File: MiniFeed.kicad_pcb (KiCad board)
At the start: 2 copper layers, 100 x 44.4 mm, 91 parts, among them J1 Debug, J2 Connector_1, J3 Uart, J4 Connector_2, M1 Motor_DC, SW1 SW_-, SW2 SW_S, SW3 SW_+, SW4 Detect1, SW5 Detect2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

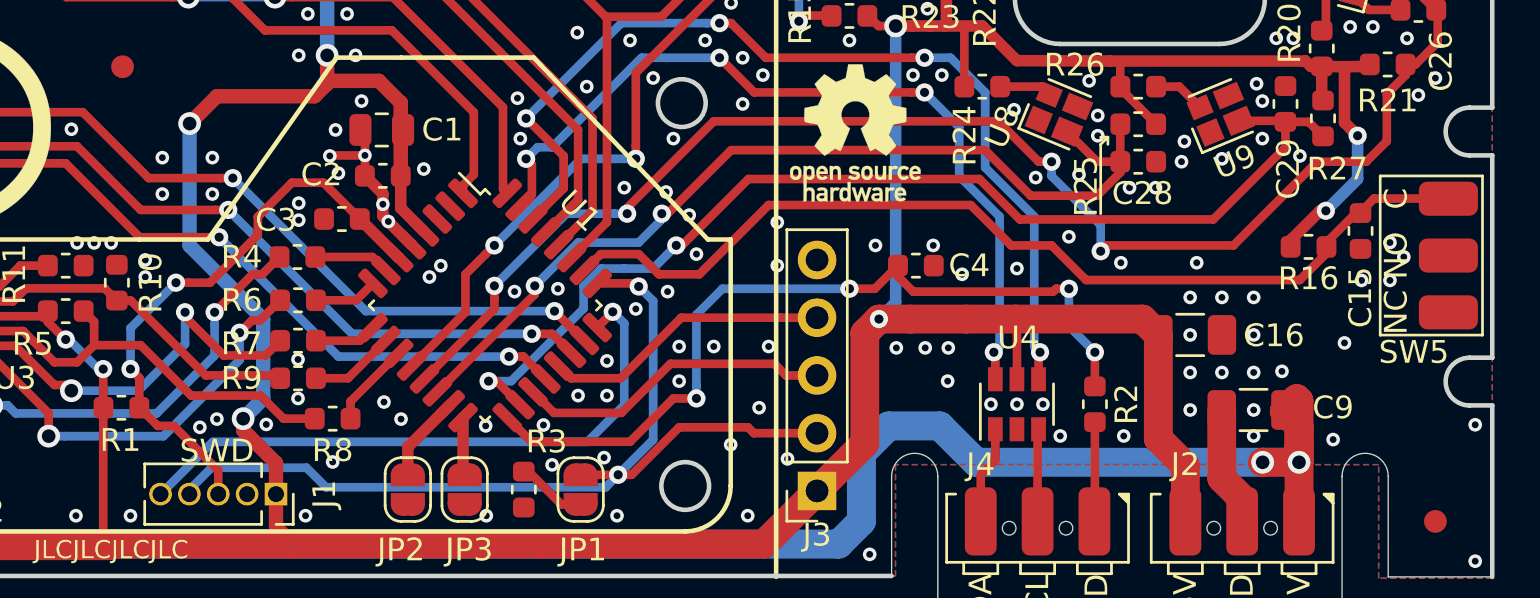
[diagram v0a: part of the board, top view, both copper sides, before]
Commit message: Added an optional power output header Changed the resistors for the VCNT2020 to improve performance
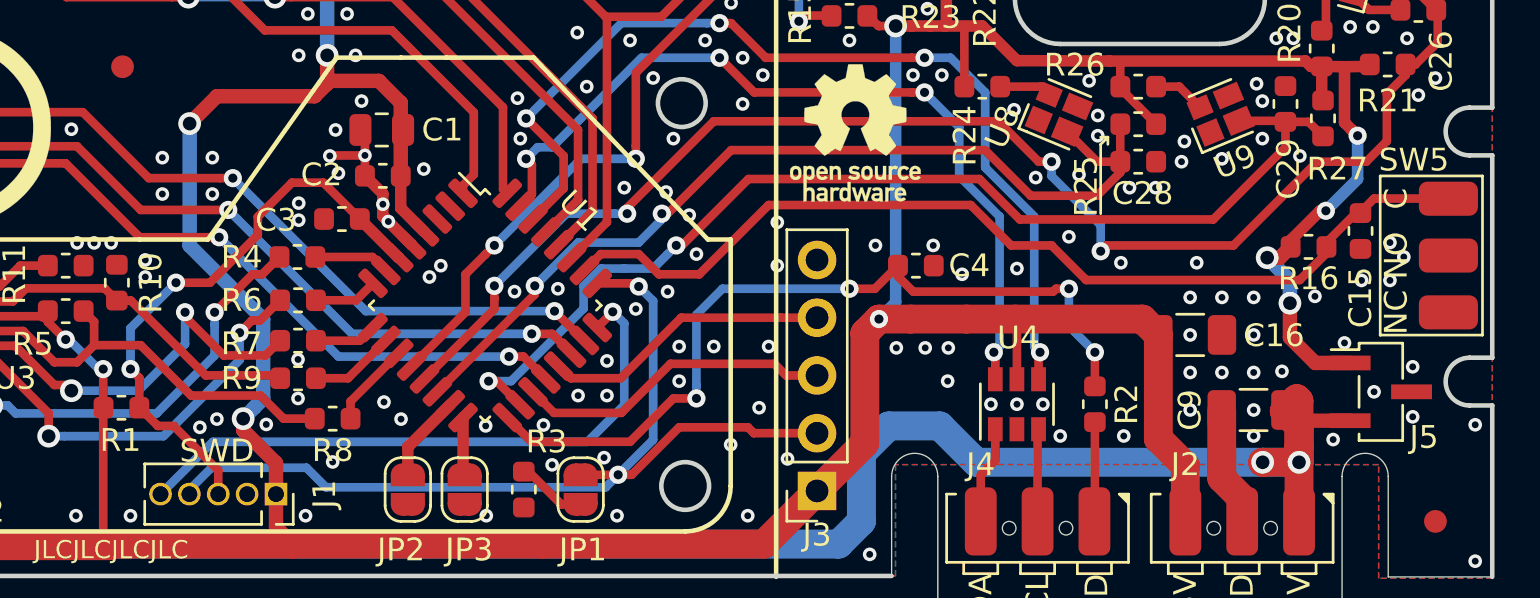
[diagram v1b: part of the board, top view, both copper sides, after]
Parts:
- added J5: PWR_Out, Connector_PinSocket_1.27mm:PinSocket_1x03_P1.27mm_Vertical_SMD_Pin1Left, F.Cu at (180.6, 100.8)
- R21, R23, R25, R27: value 10k -> 4k7
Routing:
- net +3V3: track 262.7 -> 271.0 mm, vias 10 -> 12
- net +12V: track 103.3 -> 106.3 mm
- net GND: vias 244 -> 248
